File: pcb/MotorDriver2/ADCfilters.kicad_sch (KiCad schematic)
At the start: 8 parts

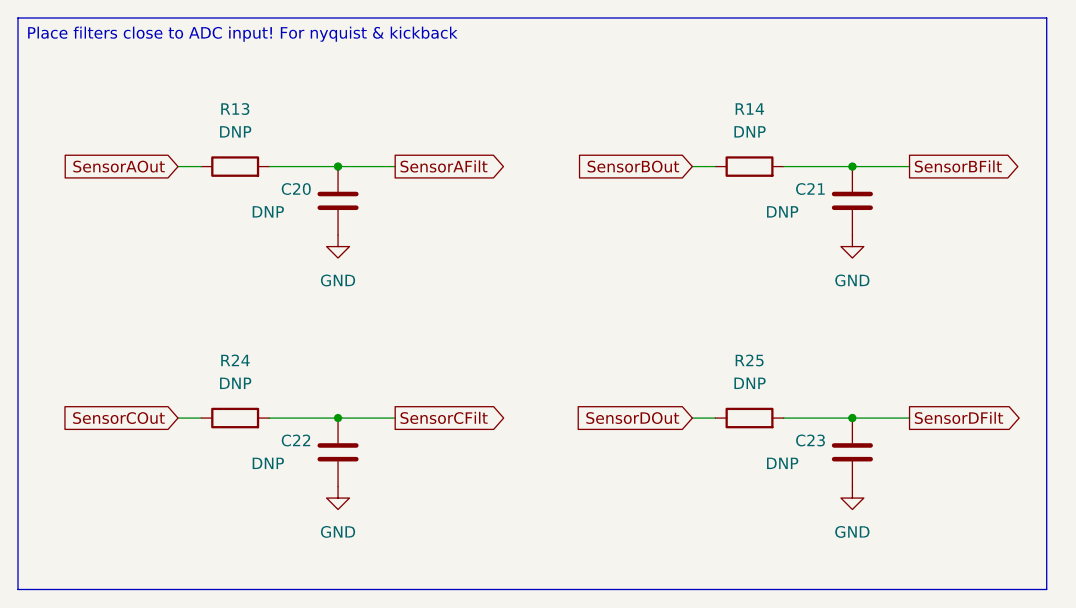
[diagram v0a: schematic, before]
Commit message: added ideal diode protection
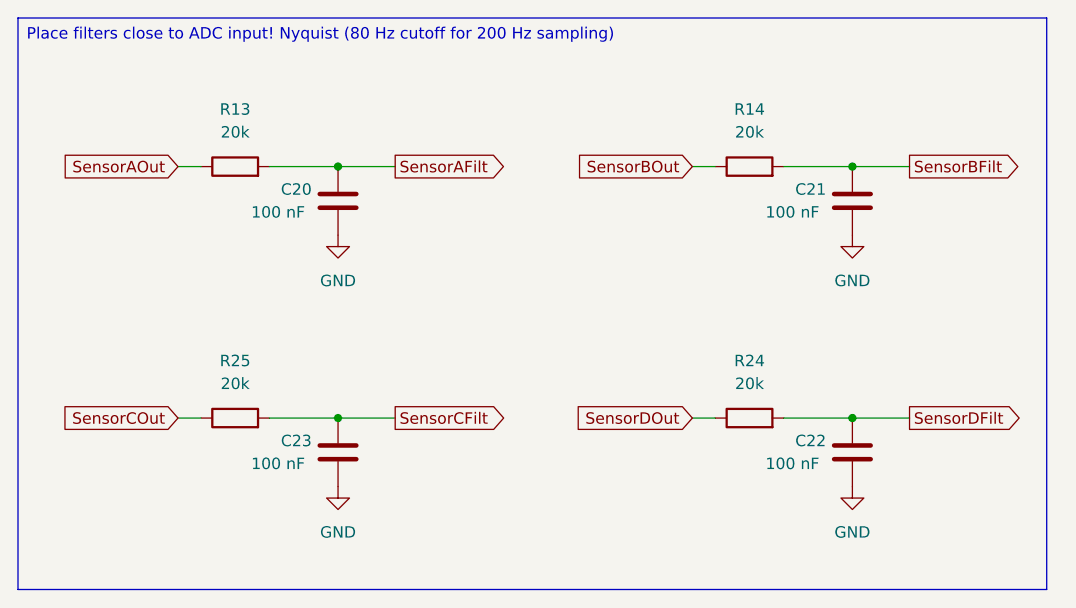
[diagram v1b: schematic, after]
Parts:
- C20, C21, C22, C23: value DNP -> 100 nF
- R13, R14, R24, R25: value DNP -> 20k
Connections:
- net SensorCFilt: now also C23.2, R25.2; no longer C22.2, R24.2
- net SensorCOut: now also R25.1; no longer R24.1
- net SensorDFilt: now also C22.2, R24.2; no longer C23.2, R25.2
- net SensorDOut: now also R24.1; no longer R25.1

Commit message: Finished pcb layout
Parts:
- C20, C21, C22, C23: footprint Capacitor_SMD:C_0603_1608Metric -> Capacitor_SMD:C_0402_1005Metric
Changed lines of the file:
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@@
 			)
 		)
-		(property "Footprint" "Capacitor_SMD:C_0603_1608Metric"
+		(property "Footprint" "Capacitor_SMD:C_0402_1005Metric"
 			(at 141.2748 60.96 0)
 			(effects
@@
 			)
 		)
-		(property "Footprint" "Capacitor_SMD:C_0603_1608Metric"
+		(property "Footprint" "Capacitor_SMD:C_0402_1005Metric"
 			(at 84.1248 60.96 0)
 			(effects
@@
 			)
 		)
-		(property "Footprint" "Capacitor_SMD:C_0603_1608Metric"
+		(property "Footprint" "Capacitor_SMD:C_0402_1005Metric"
 			(at 141.2748 88.9 0)
 			(effects
@@
 			)
 		)
-		(property "Footprint" "Capacitor_SMD:C_0603_1608Metric"
+		(property "Footprint" "Capacitor_SMD:C_0402_1005Metric"
 			(at 84.1248 88.9 0)
 			(effects
